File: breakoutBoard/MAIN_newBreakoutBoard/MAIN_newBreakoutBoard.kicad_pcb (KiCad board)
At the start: 2 copper layers, 66.9 x 18.7 mm, 3 parts, among them J1 Conn_02x06_Test_Pins, J2 Conn_02x06_Steering_Wheel_Qui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, J3 Conn_01x14

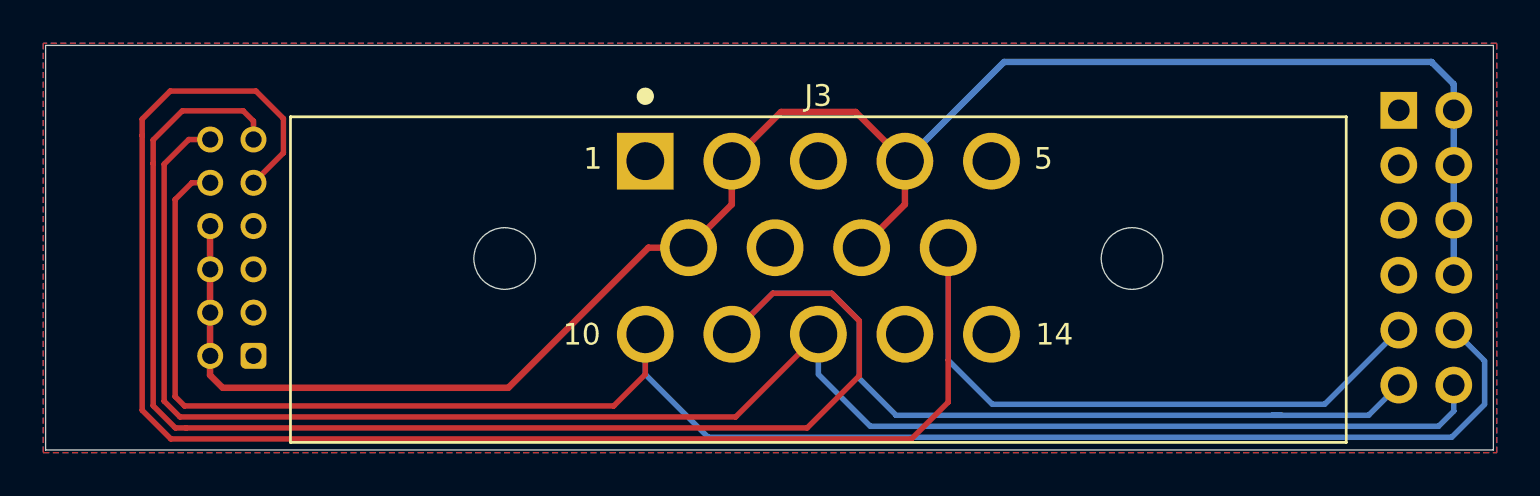
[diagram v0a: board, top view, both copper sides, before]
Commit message: Made use of entire ampseal connector
Had a late night ah ha momment;; Figured I would make use of all the pins on the ampseal connect and make it so we have the option to add another CAN node at the front of the car if need be.
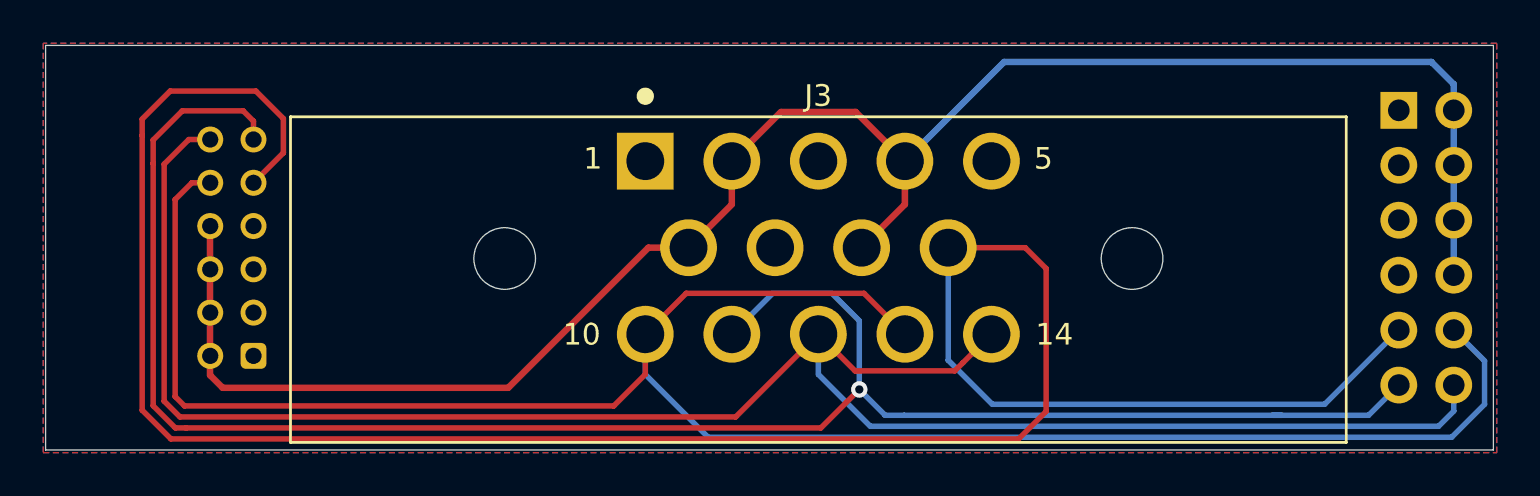
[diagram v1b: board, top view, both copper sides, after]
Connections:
- J3 pad 13: Net-(J3-Pad13) -> CAN_Low
- J3 pad 14: Net-(J3-Pad14) -> CAN_High
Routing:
- net CAN_Low: track 81.9 -> 95.5 mm
- net IMD_LED_Input: track 98.8 -> 89.1 mm, vias 0 -> 1
- net CAN_High: track 79.9 -> 89.3 mm
- net Start_Input: track 98.5 -> 107.3 mm
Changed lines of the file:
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@@
     (thickness 1.6)
     (drawings 18)
-    (tracks 87)
+    (tracks 97)
     (zones 0)
     (modules 3)
-    (nets 9)
+    (nets 7)
   )
   (page A4)
@@
   (net 5 IMD_LED_Input)
   (net 6 CAN_High)
-  (net 7 "Net-(J3-Pad13)")
-  (net 8 "Net-(J3-Pad14)")
   (net_class Default "This is the default net class."
     (clearance 0.254)
@@
     (add_net GND)
     (add_net IMD_LED_Input)
-    (add_net "Net-(J3-Pad13)")
-    (add_net "Net-(J3-Pad14)")
     (add_net Start_Input)
   )
@@
       (net 6 CAN_High))
     (pad 13 thru_hole circle (at 4 4) (size 2.625 2.625) (drill 1.75) (layers *.Cu *.Mask)
-      (net 7 "Net-(J3-Pad13)"))
+      (net 4 CAN_Low))
     (pad 14 thru_hole circle (at 8 4) (size 2.625 2.625) (drill 1.75) (layers *.Cu *.Mask)
-      (net 8 "Net-(J3-Pad14)"))
+      (net 6 CAN_High))
     (pad None np_thru_hole circle (at -14.5 0.5) (size 2.85 2.85) (drill 2.85) (layers *.Cu *.Mask))
     (pad None np_thru_hole circle (at 14.5 0.5) (size 2.85 2.85) (drill 2.85) (layers *.Cu *.Mask))
@@
   (segment (start 179.37 92.447919) (end 178.336681 91.4146) (width 0.29972) (layer B.Cu) (net 2))
   (segment (start 179.37 93.65) (end 179.37 92.447919) (width 0.29972) (layer B.Cu) (net 2))
-  (segment (start 118.744973 94.810993) (end 118.744973 107.514471) (width 0.254) (layer F.Cu) (net 3))
-  (segment (start 118.745 94.810966) (end 118.744973 94.810993) (width 0.254) (layer F.Cu) (net 3))
-  (segment (start 123.89 97) (end 125.2728 95.6172) (width 0.254) (layer F.Cu) (net 3))
-  (segment (start 124.0028 92.7608) (end 120.0404 92.7608) (width 0.254) (layer F.Cu) (net 3))
-  (segment (start 125.2728 95.6172) (end 125.2728 94.0308) (width 0.254) (layer F.Cu) (net 3))
-  (segment (start 120.0404 92.7608) (end 118.745 94.0562) (width 0.254) (layer F.Cu) (net 3))
-  (segment (start 125.2728 94.0308) (end 124.0028 92.7608) (width 0.254) (layer F.Cu) (net 3))
-  (segment (start 118.745 94.0562) (end 118.745 94.810966) (width 0.254) (layer F.Cu) (net 3))
-  (segment (start 120.069502 108.839) (end 118.744973 107.514471) (width 0.254) (layer F.Cu) (net 3))
-  (segment (start 154.305 108.839) (end 120.069502 108.839) (width 0.254) (layer F.Cu) (net 3))
-  (segment (start 156 100) (end 156 107.144) (width 0.254) (layer F.Cu) (net 3))
-  (segment (start 156 107.144) (end 154.305 108.839) (width 0.254) (layer F.Cu) (net 3))
   (segment (start 156 105.2) (end 156 100) (width 0.254) (layer B.Cu) (net 3))
   (segment (start 158.03877 107.23877) (end 156 105.2) (width 0.254) (layer B.Cu) (net 3))
   (segment (start 176.83 103.81) (end 173.40123 107.23877) (width 0.254) (layer B.Cu) (net 3))
   (segment (start 173.40123 107.23877) (end 158.03877 107.23877) (width 0.254) (layer B.Cu) (net 3))
+  (segment (start 125.2728 95.6172) (end 123.89 97) (width 0.254) (layer F.Cu) (net 3))
+  (segment (start 125.2728 94.0308) (end 125.2728 95.6172) (width 0.254) (layer F.Cu) (net 3))
+  (segment (start 124.0028 92.7608) (end 125.2728 94.0308) (width 0.254) (layer F.Cu) (net 3))
+  (segment (start 120.0404 92.7608) (end 124.0028 92.7608) (width 0.254) (layer F.Cu) (net 3))
+  (segment (start 118.745 94.0562) (end 120.0404 92.7608) (width 0.254) (layer F.Cu) (net 3))
+  (segment (start 118.745 94.810966) (end 118.745 94.0562) (width 0.254) (layer F.Cu) (net 3))
+  (segment (start 118.744973 107.514471) (end 118.744973 94.810993) (width 0.254) (layer F.Cu) (net 3))
+  (segment (start 156 100) (end 159.563 100) (width 0.254) (layer F.Cu) (net 3))
+  (segment (start 160.528 100.965) (end 160.528 107.569) (width 0.254) (layer F.Cu) (net 3))
+  (segment (start 160.528 107.569) (end 159.258 108.839) (width 0.254) (layer F.Cu) (net 3))
+  (segment (start 118.744973 94.810993) (end 118.745 94.810966) (width 0.254) (layer F.Cu) (net 3))
+  (segment (start 159.258 108.839) (end 120.069502 108.839) (width 0.254) (layer F.Cu) (net 3))
+  (segment (start 159.563 100) (end 160.528 100.965) (width 0.254) (layer F.Cu) (net 3))
+  (segment (start 120.069502 108.839) (end 118.744973 107.514471) (width 0.254) (layer F.Cu) (net 3))
   (segment (start 120.269 97.772472) (end 120.269 106.8832) (width 0.254) (layer F.Cu) (net 4))
   (segment (start 121.041472 97) (end 120.269 97.772472) (width 0.254) (layer F.Cu) (net 4))
@@
   (segment (start 179.37 103.81) (end 180.79399 105.23399) (width 0.254) (layer B.Cu) (net 4))
   (segment (start 180.79399 105.23399) (end 180.79399 107.24201) (width 0.254) (layer B.Cu) (net 4))
+  (segment (start 152.108 102.108) (end 154 104) (width 0.254) (layer F.Cu) (net 4))
+  (segment (start 142 104) (end 143.892 102.108) (width 0.254) (layer F.Cu) (net 4))
+  (segment (start 143.892 102.108) (end 152.108 102.108) (width 0.254) (layer F.Cu) (net 4))
   (segment (start 147.892 102.108) (end 150.622 102.108) (width 0.254) (layer B.Cu) (net 5))
   (segment (start 146 104) (end 147.892 102.108) (width 0.254) (layer B.Cu) (net 5))
   (segment (start 150.622 102.108) (end 151.892 103.378) (width 0.254) (layer B.Cu) (net 5))
-  (segment (start 151.892 103.378) (end 151.892 106.045) (width 0.254) (layer B.Cu) (net 5))
-  (segment (start 151.892 106.045) (end 153.59378 107.74678) (width 0.254) (layer B.Cu) (net 5))
+  (segment (start 151.892 103.378) (end 151.892 105.791) (width 0.254) (layer B.Cu) (net 5))
+  (segment (start 176.83 106.35) (end 175.43322 107.74678) (width 0.254) (layer B.Cu) (net 5))
+  (segment (start 170.99278 107.74678) (end 171.42462 107.74678) (width 0.254) (layer B.Cu) (net 5))
+  (segment (start 175.43322 107.74678) (end 170.99278 107.74678) (width 0.254) (layer B.Cu) (net 5))
+  (segment (start 151.892 105.791) (end 151.892 105.791) (width 0.254) (layer B.Cu) (net 5))
+  (segment (start 151.892 105.791) (end 151.892 106.553) (width 0.254) (layer B.Cu) (net 5))
+  (segment (start 151.892 106.553) (end 151.892 106.553) (width 0.254) (layer B.Cu) (net 5))
+  (via (at 151.892 106.553) (size 0.762) (drill 0.381) (layers F.Cu B.Cu) (net 5))
+  (segment (start 153.97478 107.74678) (end 170.99278 107.74678) (width 0.254) (layer B.Cu) (net 5))
+  (segment (start 151.892 106.553) (end 153.08578 107.74678) (width 0.254) (layer B.Cu) (net 5))
+  (segment (start 153.08578 107.74678) (end 153.97478 107.74678) (width 0.254) (layer B.Cu) (net 5))
+  (segment (start 123.89 94.151472) (end 123.89 95) (width 0.254) (layer F.Cu) (net 5))
   (segment (start 123.413728 93.6752) (end 123.89 94.151472) (width 0.254) (layer F.Cu) (net 5))
   (segment (start 120.5992 93.6752) (end 123.413728 93.6752) (width 0.254) (layer F.Cu) (net 5))
@@
   (segment (start 119.253 96.105438) (end 119.253 95.0214) (width 0.254) (layer F.Cu) (net 5))
   (segment (start 119.252981 96.105457) (end 119.253 96.105438) (width 0.254) (layer F.Cu) (net 5))
+  (segment (start 150.11401 108.33099) (end 120.77701 108.33099) (width 0.254) (layer F.Cu) (net 5))
+  (segment (start 151.892 106.553) (end 150.11401 108.33099) (width 0.254) (layer F.Cu) (net 5))
+  (segment (start 120.77701 108.33099) (end 120.777 108.331) (width 0.254) (layer F.Cu) (net 5))
+  (segment (start 120.777 108.331) (end 120.279934 108.331) (width 0.254) (layer F.Cu) (net 5))
+  (segment (start 120.279934 108.331) (end 119.252982 107.304048) (width 0.254) (layer F.Cu) (net 5))
   (segment (start 119.252982 107.304048) (end 119.252981 96.105457) (width 0.254) (layer F.Cu) (net 5))
-  (segment (start 120.279934 108.331) (end 119.252982 107.304048) (width 0.254) (layer F.Cu) (net 5))
-  (segment (start 120.777 108.331) (end 120.279934 108.331) (width 0.254) (layer F.Cu) (net 5))
-  (segment (start 120.77701 108.33099) (end 120.777 108.331) (width 0.254) (layer F.Cu) (net 5))
-  (segment (start 146 104) (end 147.892 102.108) (width 0.254) (layer F.Cu) (net 5))
-  (segment (start 150.614382 102.108) (end 151.892 103.385618) (width 0.254) (layer F.Cu) (net 5))
-  (segment (start 151.892 103.385618) (end 151.892 105.918) (width 0.254) (layer F.Cu) (net 5))
-  (segment (start 147.892 102.108) (end 150.614382 102.108) (width 0.254) (layer F.Cu) (net 5))
-  (segment (start 151.892 105.918) (end 149.47901 108.33099) (width 0.254) (layer F.Cu) (net 5))
-  (segment (start 123.89 94.151472) (end 123.89 95) (width 0.254) (layer F.Cu) (net 5))
-  (segment (start 149.47901 108.33099) (end 120.77701 108.33099) (width 0.254) (layer F.Cu) (net 5))
-  (segment (start 176.83 106.35) (end 175.43322 107.74678) (width 0.254) (layer B.Cu) (net 5))
-  (segment (start 153.59378 107.74678) (end 170.99278 107.74678) (width 0.254) (layer B.Cu) (net 5))
-  (segment (start 170.99278 107.74678) (end 171.42462 107.74678) (width 0.254) (layer B.Cu) (net 5))
-  (segment (start 175.43322 107.74678) (end 170.99278 107.74678) (width 0.254) (layer B.Cu) (net 5))
   (segment (start 120.9 95) (end 121.89 95) (width 0.254) (layer F.Cu) (net 6))
   (segment (start 119.76099 96.13901) (end 120.9 95) (width 0.254) (layer F.Cu) (net 6))
@@
   (segment (start 179.37 107.552081) (end 178.667291 108.25479) (width 0.254) (layer B.Cu) (net 6))
   (segment (start 179.37 106.35) (end 179.37 107.552081) (width 0.254) (layer B.Cu) (net 6))
+  (segment (start 156.687501 105.312499) (end 158 104) (width 0.254) (layer F.Cu) (net 6))
+  (segment (start 156.306499 105.693501) (end 156.687501 105.312499) (width 0.254) (layer F.Cu) (net 6))
+  (segment (start 151.693501 105.693501) (end 156.306499 105.693501) (width 0.254) (layer F.Cu) (net 6))
+  (segment (start 150 104) (end 151.693501 105.693501) (width 0.254) (layer F.Cu) (net 6))
   (zone (net 1) (net_name GND) (layer F.Cu) (hatch edge 0.508)
     (connect_pads (clearance 0.508))
